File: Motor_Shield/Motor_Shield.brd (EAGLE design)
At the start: 54.6 x 39.7 mm, 12 parts, among them IC1 7805T, IC2 L293D

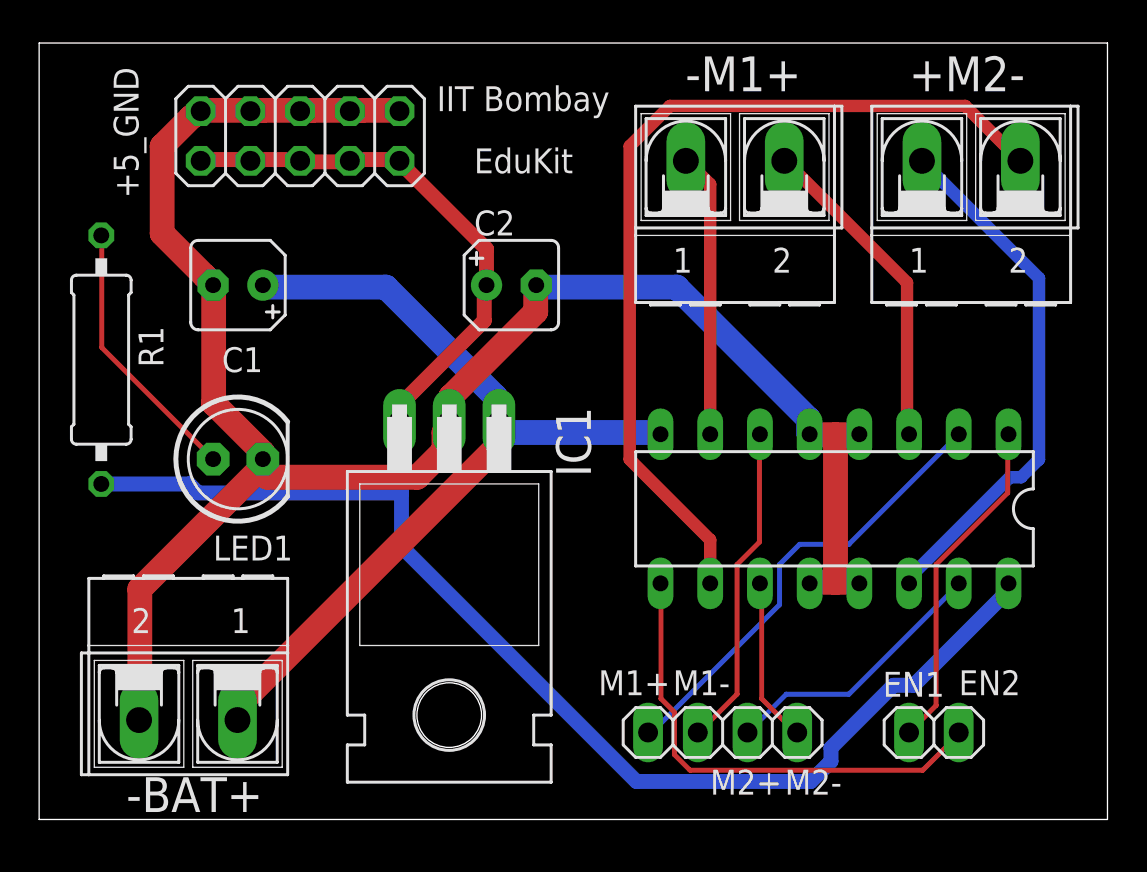
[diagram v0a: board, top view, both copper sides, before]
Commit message: Changed Net Classes
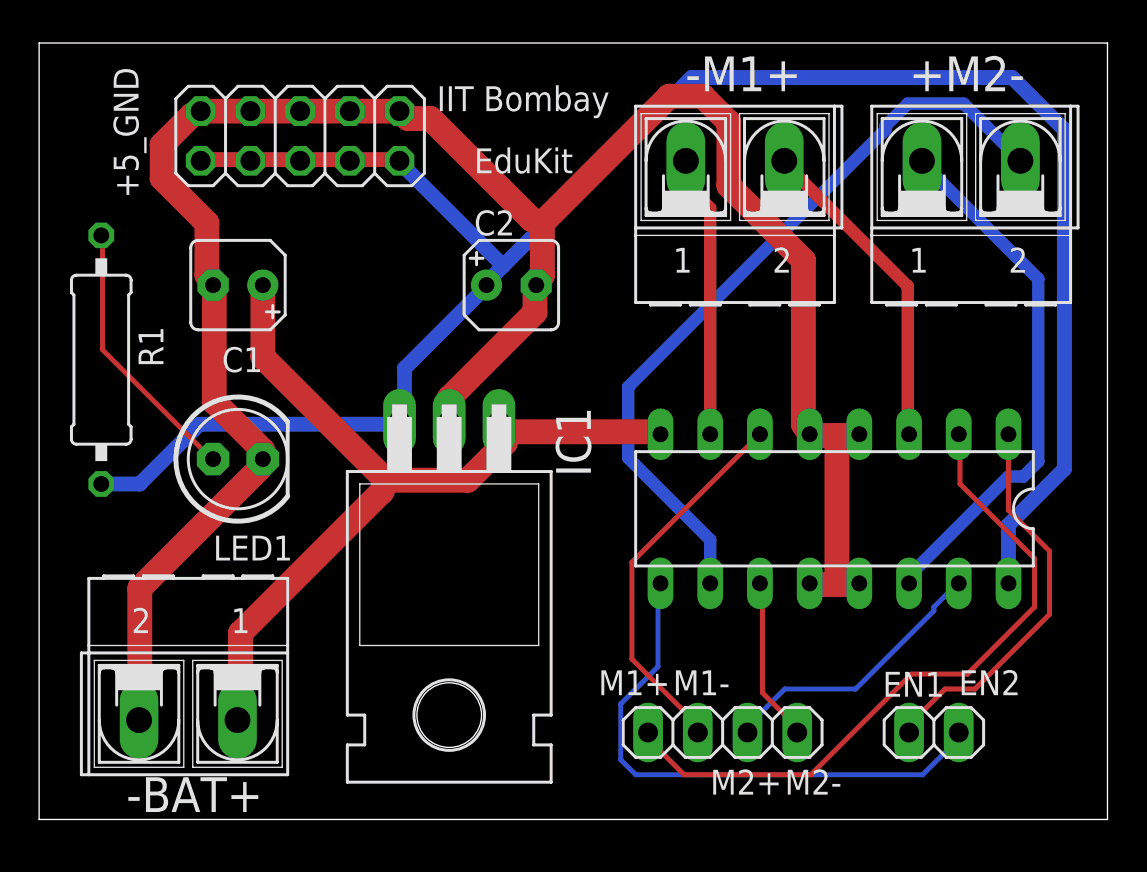
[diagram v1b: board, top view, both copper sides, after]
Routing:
- net GND: track 97.6 -> 111.8 mm
- net +5V: track 90.1 -> 102.7 mm
- net M1+: track 23.5 -> 34.8 mm
- net MOTOR2_-: track 46.0 -> 39.1 mm
- net EN2: track 24.7 -> 28.6 mm
- net M1-: track 16.6 -> 19.3 mm
- net EN1: track 17.3 -> 20.0 mm
